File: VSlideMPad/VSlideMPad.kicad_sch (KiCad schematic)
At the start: 1 part

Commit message: start of thingnymabob
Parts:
- added R1, R2, R3: P120PK-Y25BR10K, VSlideMPad:POT_P120PK-x25_TTE, symbol POT_P120PK-x25_TTE:P120PK-Y25BR10K
- added R5, R6, R7: PTA4543-2015DPB103, PTA4543-2015DPB103:TRIM_PTA4543-2015DPB103, symbol PTA4543-2015DPB103:PTA4543-2015DPB103

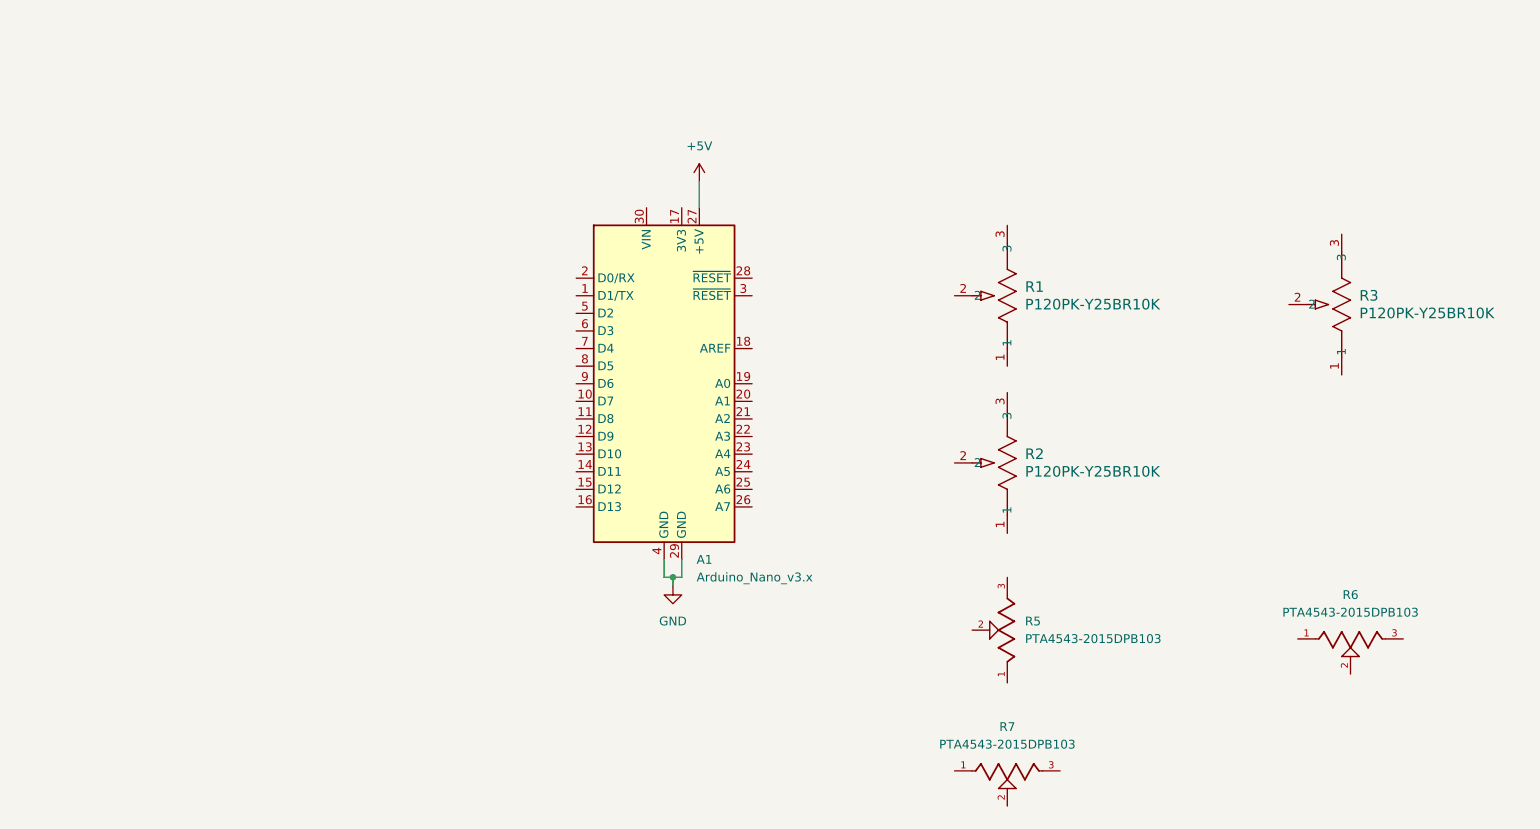
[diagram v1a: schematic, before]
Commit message: added pot
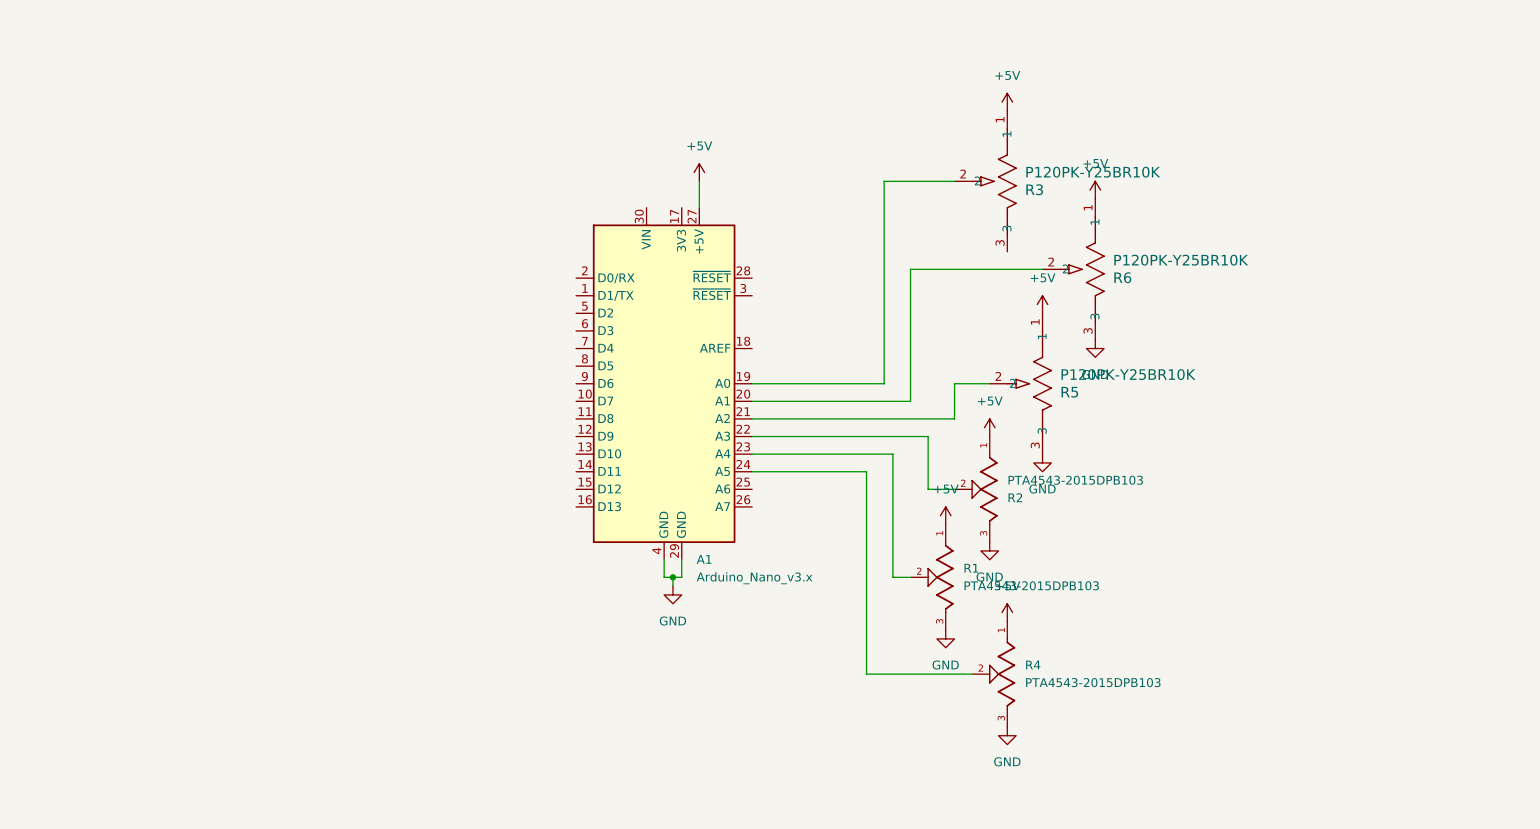
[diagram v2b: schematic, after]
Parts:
- removed R3: P120PK-Y25BR10K, VSlideMPad:POT_P120PK-x25_TTE, symbol POT_P120PK-x25_TTE:P120PK-Y25BR10K
- removed R6, R7: PTA4543-2015DPB103, PTA4543-2015DPB103:TRIM_PTA4543-2015DPB103, symbol PTA4543-2015DPB103:PTA4543-2015DPB103
- added R1, R4: PTA4543-2015DPB103, PTA4543-2015DPB103:TRIM_PTA4543-2015DPB103, symbol PTA4543-2015DPB103:PTA4543-2015DPB103
- added R5: P120PK-Y25BR10K, POT_P120PK-x25_TTE, symbol POT_P120PK-x25_TTE:P120PK-Y25BR10K
- R3: renamed from R1; footprint VSlideMPad:POT_P120PK-x25_TTE -> POT_P120PK-x25_TTE
- R6: renamed from R2; footprint VSlideMPad:POT_P120PK-x25_TTE -> POT_P120PK-x25_TTE
- renumbered R5 to R2
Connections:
- net +5V: now also R2.1, R3.1, R6.1, R1.1, R4.1, R5.1
- net GND: now also R2.3, R6.3, R1.3, R4.3, R5.3
- net at R3.2: now also A1.19 (A0)
- net at A1.20 (A1): now also R6.2
- net at A1.21 (A2): now also R5.2
- net at A1.22 (A3): now also R2.2
- net at A1.23 (A4): now also R1.2
- net at A1.24 (A5): now also R4.2
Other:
- moved on the sheet: R2, R3, R6

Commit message: fixed added cherry switches and fixed potentiometres
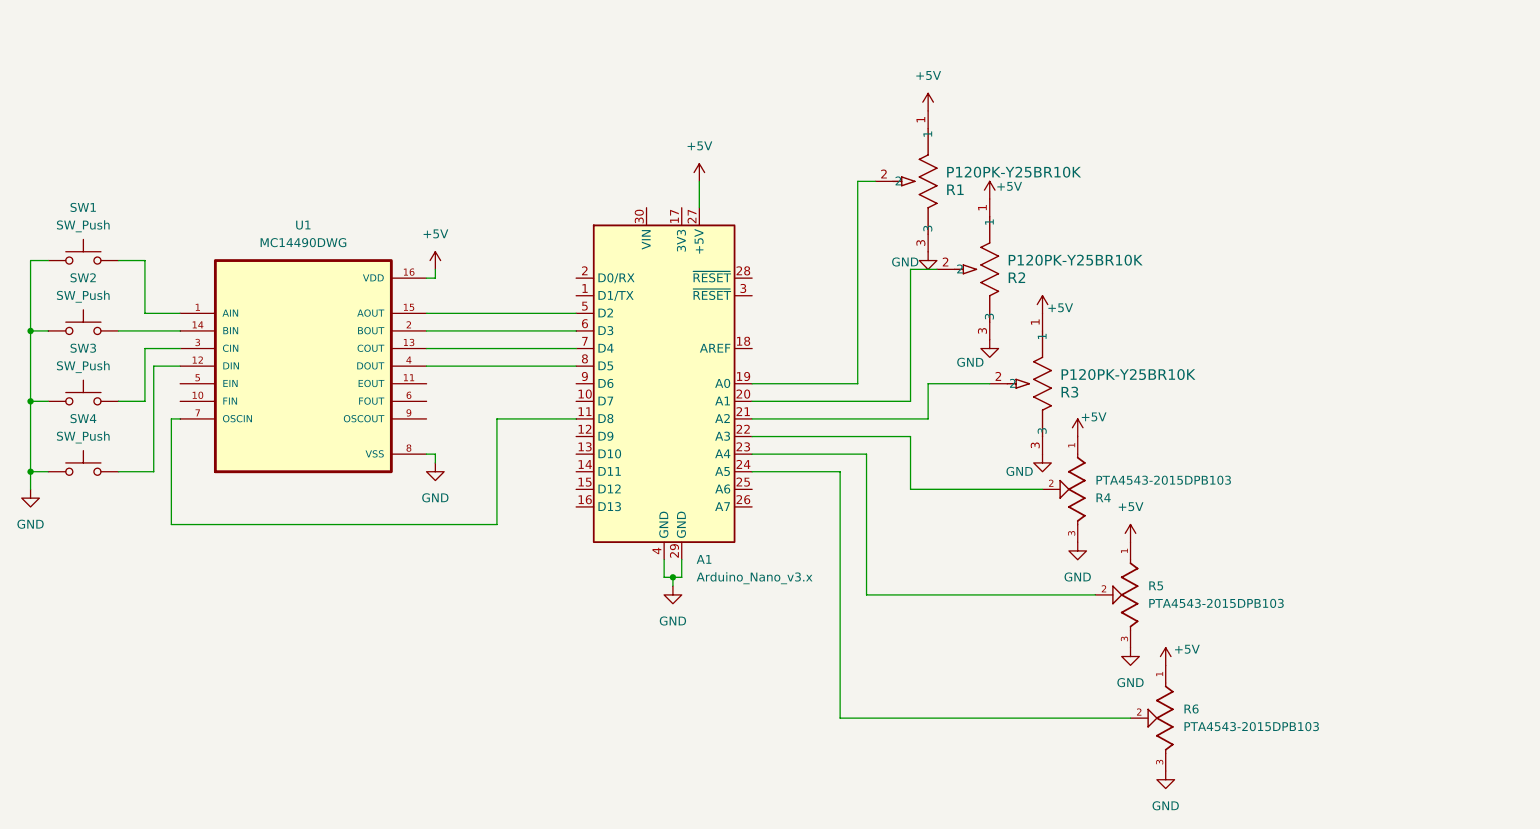
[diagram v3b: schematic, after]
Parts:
- added SW1, SW2, SW3, SW4: SW_Push, Switch_Keyboard_Cherry_MX:SW_Cherry_MX_PCB_1.00u, symbol Switch:SW_Push
- added U1: MC14490DWG, MC14490DWG:SOIC127P1030X265-16N, symbol MC14490DWG:MC14490DWG
- R1: renamed from R3; footprint POT_P120PK-x25_TTE -> POT_P120PK-x25_TTE:POT_P120PK-x25_TTE
- R2: renamed from R6; footprint POT_P120PK-x25_TTE -> POT_P120PK-x25_TTE:POT_P120PK-x25_TTE
- R3: renamed from R5; footprint POT_P120PK-x25_TTE -> POT_P120PK-x25_TTE:POT_P120PK-x25_TTE
- renumbered R2 to R4, R1 to R5, R4 to R6
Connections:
- net +5V: now also U1.16 (VDD)
- net GND: now also R1.3, SW1.1, SW2.1, SW3.1, SW4.1, U1.8 (VSS)
- net at A1.11 (D8): now also U1.7 (OSCIN)
- net at A1.5 (D2): now also U1.15 (AOUT)
- net at A1.6 (D3): now also U1.2 (BOUT)
- net at A1.7 (D4): now also U1.13 (COUT)
- net at A1.8 (D5): now also U1.4 (DOUT)
- new net: SW4.2, U1.12 (DIN)
- new net: SW1.2, U1.1 (AIN)
- new net: SW2.2, U1.14 (BIN)
- new net: SW3.2, U1.3 (CIN)
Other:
- moved on the sheet: R1, R2, R4, R5, R6

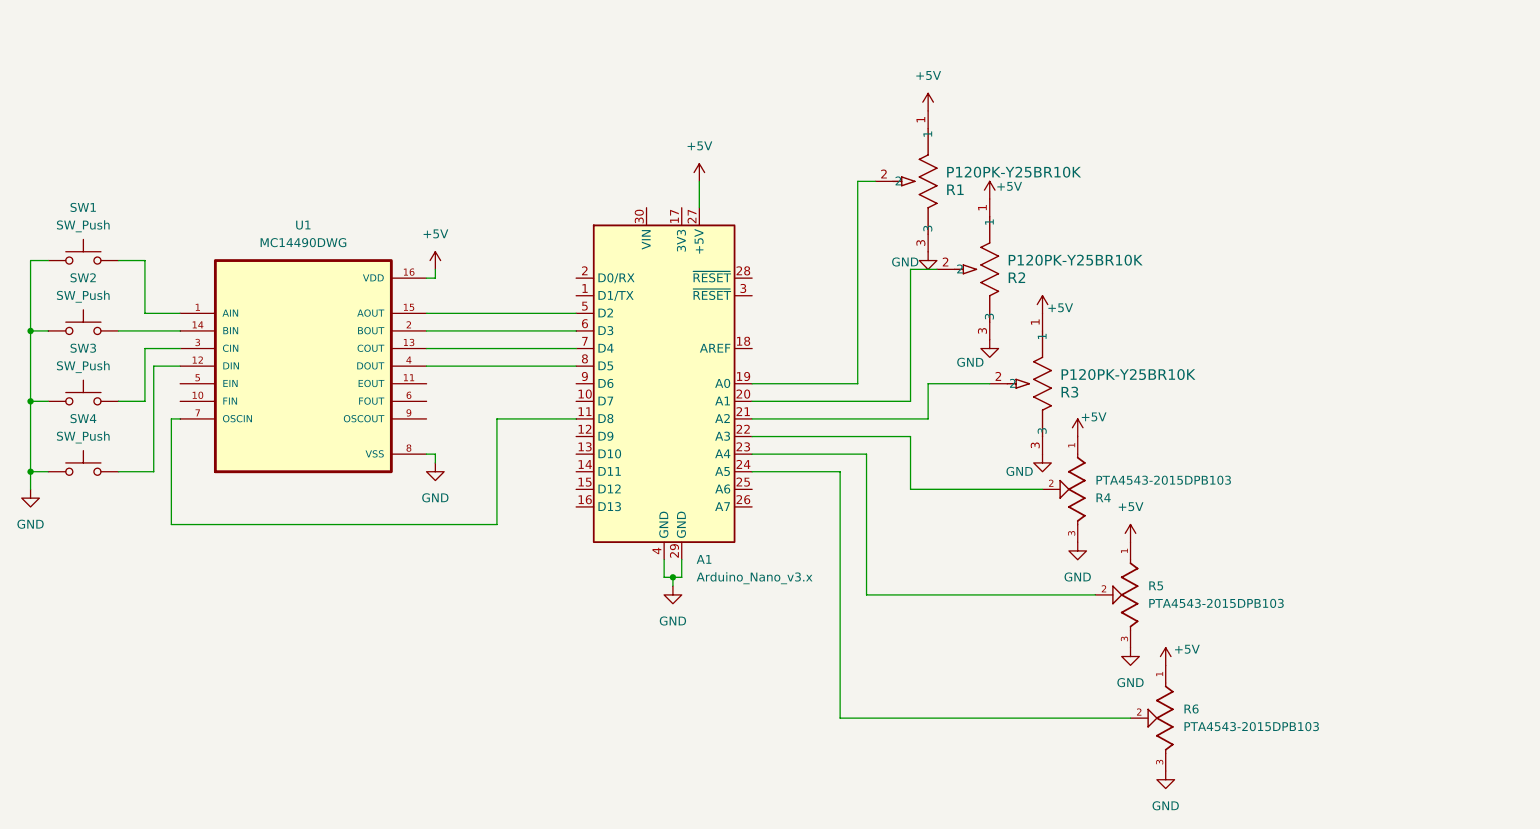
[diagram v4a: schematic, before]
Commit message: ajout cap mc44040
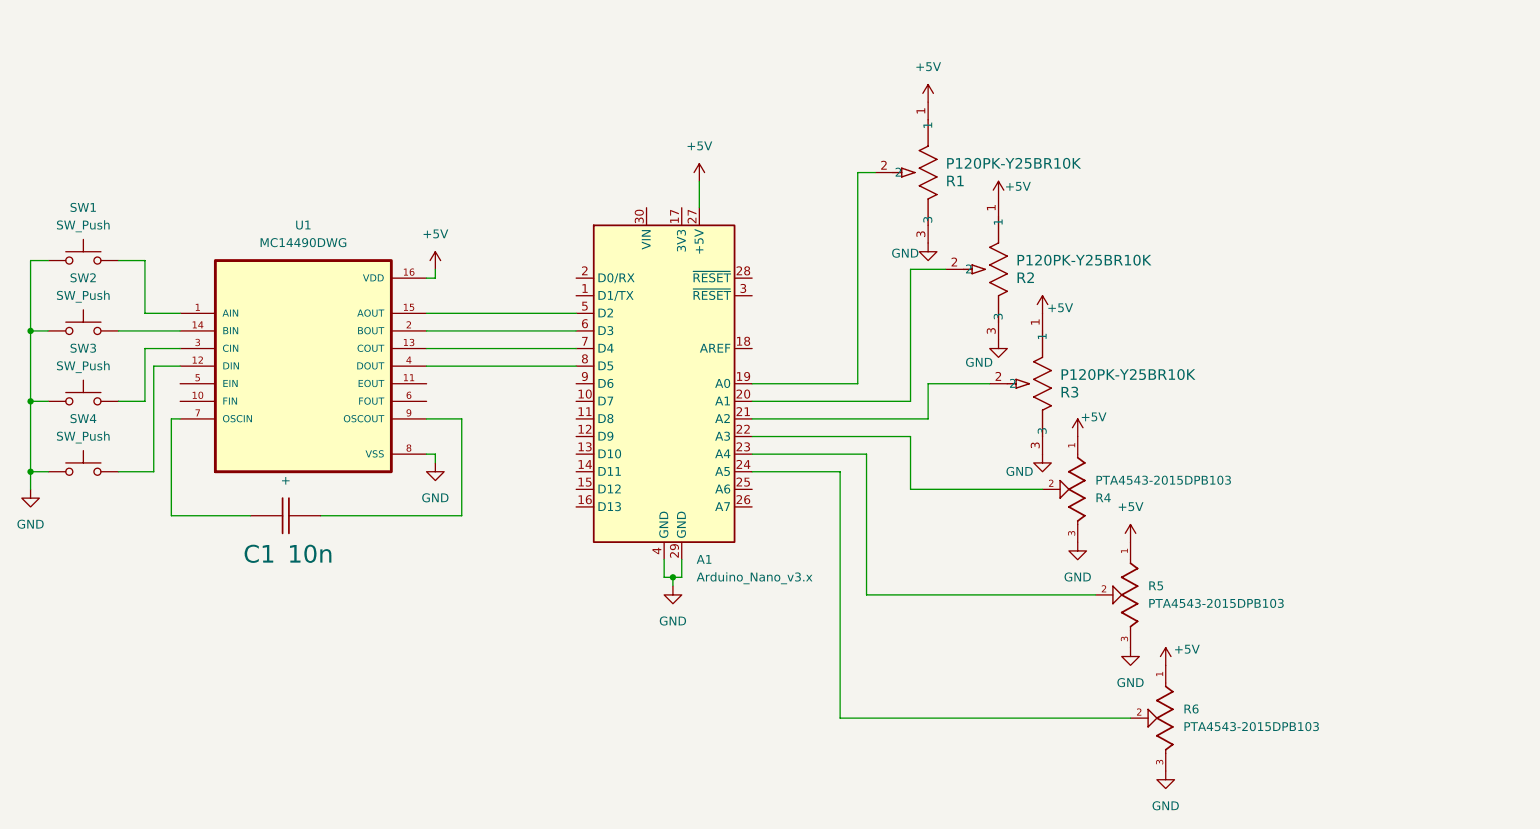
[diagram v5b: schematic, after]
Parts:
- added C1: 10n, 4ms_Capacitor:C_1206, symbol Generic:C,IEC
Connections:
- net at U1.7 (OSCIN): now also C1.1 (+); no longer A1.11 (D8)
- net at U1.9 (OSCOUT): now also C1.2 (-)
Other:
- moved on the sheet: R1, R2
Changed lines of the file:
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@@
 	(wire
 		(pts
-			(xy 177.8 55.88) (xy 177.8 85.09)
-		)
-		(stroke
-			(width 0)
-			(type default)
-		)
-	)
-	(wire
-		(pts
-			(xy 125.73 105.41) (xy 125.73 90.17)
+			(xy 177.8 54.61) (xy 177.8 85.09)
 		)
 		(stroke
@@
 	(wire
 		(pts
-			(xy 78.74 90.17) (xy 78.74 105.41)
+			(xy 120.65 104.14) (xy 120.65 90.17)
+		)
+		(stroke
+			(width 0)
+			(type default)
+		)
+	)
+	(wire
+		(pts
+			(xy 78.74 90.17) (xy 78.74 104.14)
 		)
 		(stroke
@@
 	(wire
 		(pts
+			(xy 100.33 104.14) (xy 120.65 104.14)
+		)
+		(stroke
+			(width 0)
+			(type default)
+		)
+	)
+	(wire
+		(pts
 			(xy 58.42 77.47) (xy 58.42 67.31)
 		)
@@
 	(wire
 		(pts
+			(xy 78.74 104.14) (xy 90.17 104.14)
+		)
+		(stroke
+			(width 0)
+			(type default)
+		)
+	)
+	(wire
+		(pts
 			(xy 76.2 97.79) (xy 71.12 97.79)
 		)
@@
 	(wire
 		(pts
-			(xy 78.74 105.41) (xy 125.73 105.41)
-		)
-		(stroke
-			(width 0)
-			(type default)
-		)
-	)
-	(wire
-		(pts
-			(xy 125.73 90.17) (xy 137.16 90.17)
-		)
-		(stroke
-			(width 0)
-			(type default)
-		)
-	)
-	(wire
-		(pts
-			(xy 185.42 68.58) (xy 189.23 68.58)
+			(xy 185.42 68.58) (xy 190.5 68.58)
 		)
 		(stroke
@@
 	(wire
 		(pts
+			(xy 120.65 90.17) (xy 115.57 90.17)
+		)
+		(stroke
+			(width 0)
+			(type default)
+		)
+	)
+	(wire
+		(pts
 			(xy 179.07 115.57) (xy 212.09 115.57)
 		)
@@
 	(wire
 		(pts
-			(xy 180.34 55.88) (xy 177.8 55.88)
+			(xy 180.34 54.61) (xy 177.8 54.61)
 		)
 		(stroke
@@
 	(symbol
 		(lib_id "POT_P120PK-x25_TTE:P120PK-Y25BR10K")
-		(at 187.96 45.72 90)
+		(at 187.96 44.45 90)
 		(mirror x)
 		(unit 1)
@@
 		(dnp no)
 		(property "Reference" "R1"
-			(at 190.5 57.1501 90)
+			(at 190.5 55.8801 90)
 			(effects
 				(font
@@
 		)
 		(property "Value" "P120PK-Y25BR10K"
-			(at 190.5 54.6101 90)
+			(at 190.5 53.3401 90)
 			(effects
 				(font
@@
 		)
 		(property "Footprint" "POT_P120PK-x25_TTE:POT_P120PK-x25_TTE"
-			(at 187.96 45.72 0)
+			(at 187.96 44.45 0)
 			(effects
 				(font
@@
 		)
 		(property "Datasheet" "P120PK-Y25BR10K"
-			(at 187.96 45.72 0)
+			(at 187.96 44.45 0)
 			(effects
 				(font
@@
 		)
 		(property "Description" ""
-			(at 187.96 45.72 0)
+			(at 187.96 44.45 0)
 			(effects
 				(font
@@
 	(symbol
 		(lib_id "power:GND")
-		(at 196.85 78.74 0)
+		(at 198.12 78.74 0)
 		(unit 1)
 		(exclude_from_sim no)
@@
 		(dnp no)
 		(property "Reference" "#PWR07"
-			(at 196.85 85.09 0)
+			(at 198.12 85.09 0)
 			(effects
 				(font
@@
 		)
 		(property "Value" "GND"
-			(at 194.056 82.042 0)
+			(at 195.326 82.042 0)
 			(effects
 				(font
@@
 		)
 		(property "Footprint" ""
-			(at 196.85 78.74 0)
+			(at 198.12 78.74 0)
 			(effects
 				(font
@@
 		)
 		(property "Datasheet" ""
-			(at 196.85 78.74 0)
+			(at 198.12 78.74 0)
 			(effects
 				(font
@@
 		)
 		(property "Description" "Power symbol creates a global label with name \"GND\" , ground"
-			(at 196.85 78.74 0)
+			(at 198.12 78.74 0)
 			(effects
 				(font
@@
 	(symbol
 		(lib_id "power:+5V")
-		(at 196.85 58.42 0)
+		(at 198.12 58.42 0)
 		(unit 1)
 		(exclude_from_sim no)
@@
 		(dnp no)
 		(property "Reference" "#PWR03"
-			(at 196.85 62.23 0)
+			(at 198.12 62.23 0)
 			(effects
 				(font
@@
 		)
 		(property "Value" "+5V"
-			(at 199.644 56.642 0)
+			(at 200.914 56.642 0)
 			(effects
 				(font
@@
 		)
 		(property "Footprint" ""
-			(at 196.85 58.42 0)
+			(at 198.12 58.42 0)
 			(effects
 				(font
@@
 		)
 		(property "Datasheet" ""
-			(at 196.85 58.42 0)
+			(at 198.12 58.42 0)
 			(effects
 				(font
@@
 		)
 		(property "Description" "Power symbol creates a global label with name \"+5V\""
-			(at 196.85 58.42 0)
+			(at 198.12 58.42 0)
 			(effects
 				(font
@@
 				(path "/8ba016b1-0249-4304-9ab0-63c4f54fb05f"
 					(reference "A1")
+					(unit 1)
+				)
+			)
+		)
+	)
+	(symbol
+		(lib_id "Generic:C,IEC")
+		(at 95.25 104.14 90)
+		(unit 1)
+		(exclude_from_sim no)
+		(in_bom yes)
+		(on_board yes)
+		(dnp no)
+		(property "Reference" "C1"
+			(at 91.44 109.728 90)
+			(effects
+				(font
+					(size 2.54 2.54)
+				)
+			)
+		)
+		(property "Value" "10n"
+			(at 98.806 109.728 90)
+			(effects
+				(font
+					(size 2.54 2.54)
+				)
+			)
+		)
+		(property "Footprint" "4ms_Capacitor:C_1206"
+			(at 95.25 104.14 0)
+			(effects
+				(font
+					(size 2.54 2.54)
+				)
+				(hide yes)
+			)
+		)
+		(property "Datasheet" ""
+			(at 95.25 104.14 0)
+			(effects
+				(font
+					(size 2.54 2.54)
+				)
+				(hide yes)
+			)
+		)
+		(property "Description" "capacitor, non-polarized/polar(ized)/bipolar (IEC)"
+			(at 95.25 104.14 0)
+			(effects
+				(font
+					(size 1.27 1.27)
+				)
+				(hide yes)
+			)
+		)
+		(property "Indicator" "+"
+			(at 95.25 99.06 90)
+			(effects
+				(font
+					(size 1.27 1.27)
+				)
+			)
+		)
+		(pin "1"
+		)
+		(pin "2"
+		)
+		(instances
+			(project ""
+				(path "/8ba016b1-0249-4304-9ab0-63c4f54fb05f"
+					(reference "C1")
 					(unit 1)
 				)
@@
 	(symbol
 		(lib_id "POT_P120PK-x25_TTE:P120PK-Y25BR10K")
-		(at 196.85 58.42 90)
+		(at 198.12 58.42 90)
 		(mirror x)
 		(unit 1)
@@
 		(dnp no)
 		(property "Reference" "R2"
-			(at 199.39 69.8501 90)
+			(at 200.66 69.8501 90)
 			(effects
 				(font
@@
 		)
 		(property "Value" "P120PK-Y25BR10K"
-			(at 199.39 67.3101 90)
+			(at 200.66 67.3101 90)
 			(effects
 				(font
@@
 		)
 		(property "Footprint" "POT_P120PK-x25_TTE:POT_P120PK-x25_TTE"
-			(at 196.85 58.42 0)
+			(at 198.12 58.42 0)
 			(effects
 				(font
@@
 		)
 		(property "Datasheet" "P120PK-Y25BR10K"
-			(at 196.85 58.42 0)
+			(at 198.12 58.42 0)
 			(effects
 				(font
@@
 		)
 		(property "Description" ""
-			(at 196.85 58.42 0)
+			(at 198.12 58.42 0)
 			(effects
 				(font
@@
 	(symbol
 		(lib_id "power:+5V")
-		(at 187.96 45.72 0)
+		(at 187.96 44.45 0)
 		(unit 1)
 		(exclude_from_sim no)
@@
 		(fields_autoplaced yes)
 		(property "Reference" "#PWR01"
-			(at 187.96 49.53 0)
+			(at 187.96 48.26 0)
 			(effects
 				(font
@@
 		)
 		(property "Value" "+5V"
-			(at 187.96 40.64 0)
+			(at 187.96 39.37 0)
 			(effects
 				(font
@@
 		)
 		(property "Footprint" ""
-			(at 187.96 45.72 0)
+			(at 187.96 44.45 0)
 			(effects
 				(font
@@
 		)
 		(property "Datasheet" ""
-			(at 187.96 45.72 0)
+			(at 187.96 44.45 0)
 			(effects
 				(font
@@
 		)
 		(property "Description" "Power symbol creates a global label with name \"+5V\""
-			(at 187.96 45.72 0)
+			(at 187.96 44.45 0)
 			(effects
 				(font
@@
 	(symbol
 		(lib_id "power:GND")
-		(at 187.96 66.04 0)
+		(at 187.96 64.77 0)
 		(unit 1)
 		(exclude_from_sim no)
@@
 		(dnp no)
 		(property "Reference" "#PWR04"
-			(at 187.96 72.39 0)
+			(at 187.96 71.12 0)
 			(effects
 				(font
@@
 		)
 		(property "Value" "GND"
-			(at 184.658 67.564 0)
+			(at 184.658 66.294 0)
 			(effects
 				(font
@@
 		)
 		(property "Footprint" ""
-			(at 187.96 66.04 0)
+			(at 187.96 64.77 0)
 			(effects
 				(font
@@
 		)
 		(property "Datasheet" ""
-			(at 187.96 66.04 0)
+			(at 187.96 64.77 0)
 			(effects
 				(font
@@
 		)
 		(property "Description" "Power symbol creates a global label with name \"GND\" , ground"
-			(at 187.96 66.04 0)
-			(effects
-				(font
+			(at 187.96 64.77 0)
+			(effects
+				(font
